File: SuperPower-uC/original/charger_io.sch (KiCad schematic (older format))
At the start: 21 parts, among them J2 Barrel_Jack_Switch, J3 Conn_01x02_Male, Q2 DMP3028LSD, U2 USB-C, U3 IP4220CZ6

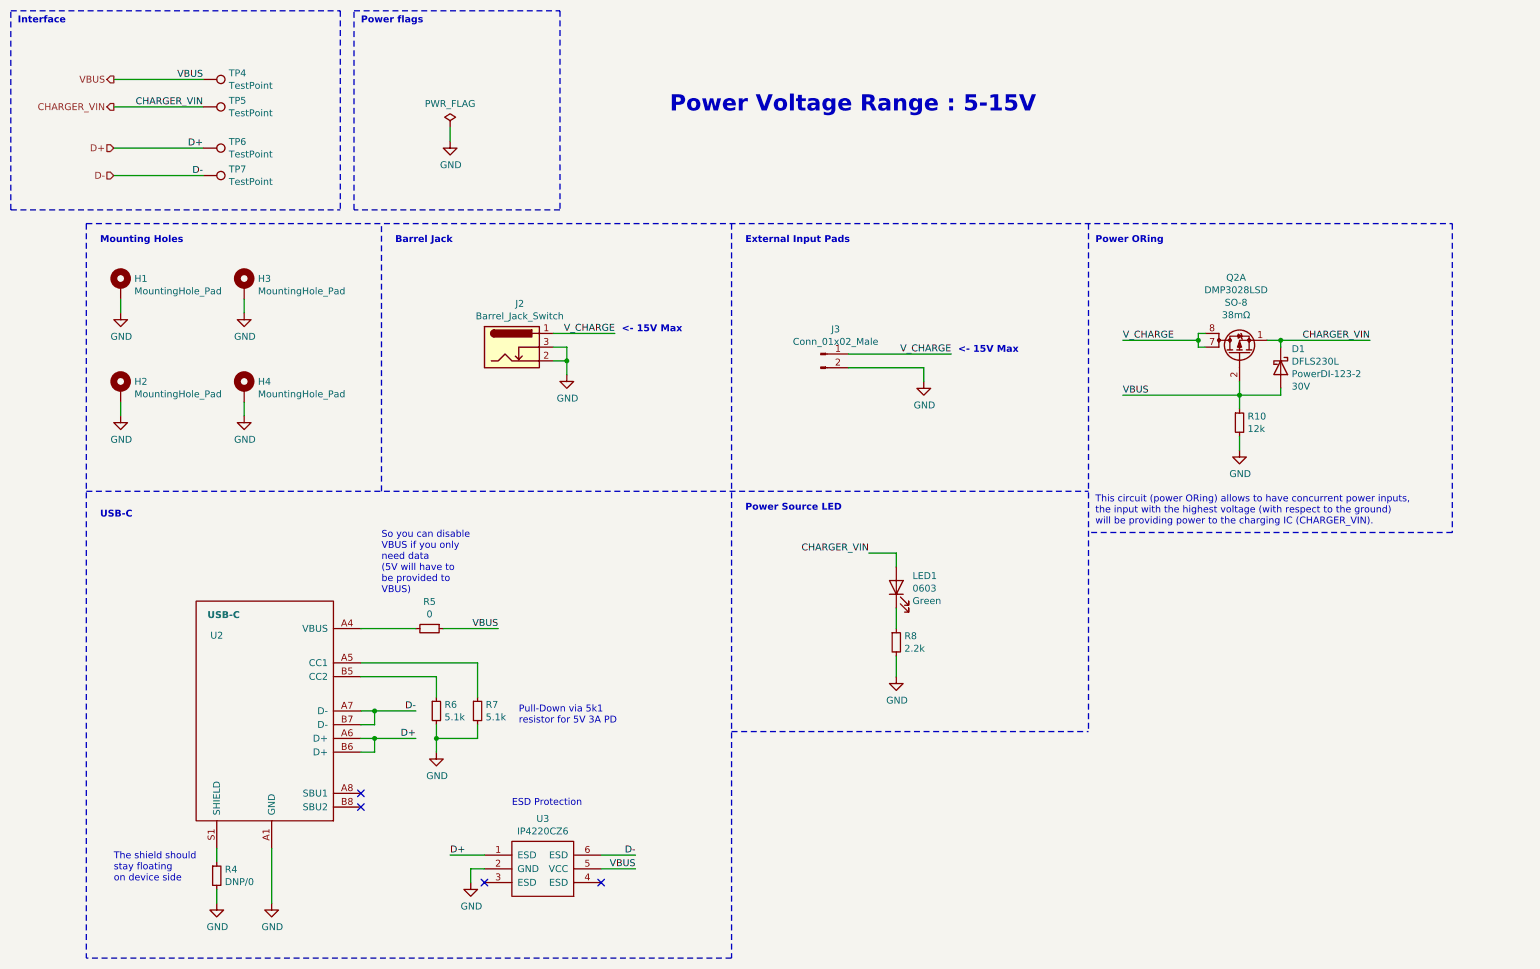
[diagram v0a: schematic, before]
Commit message: Layed out IO sheet parts
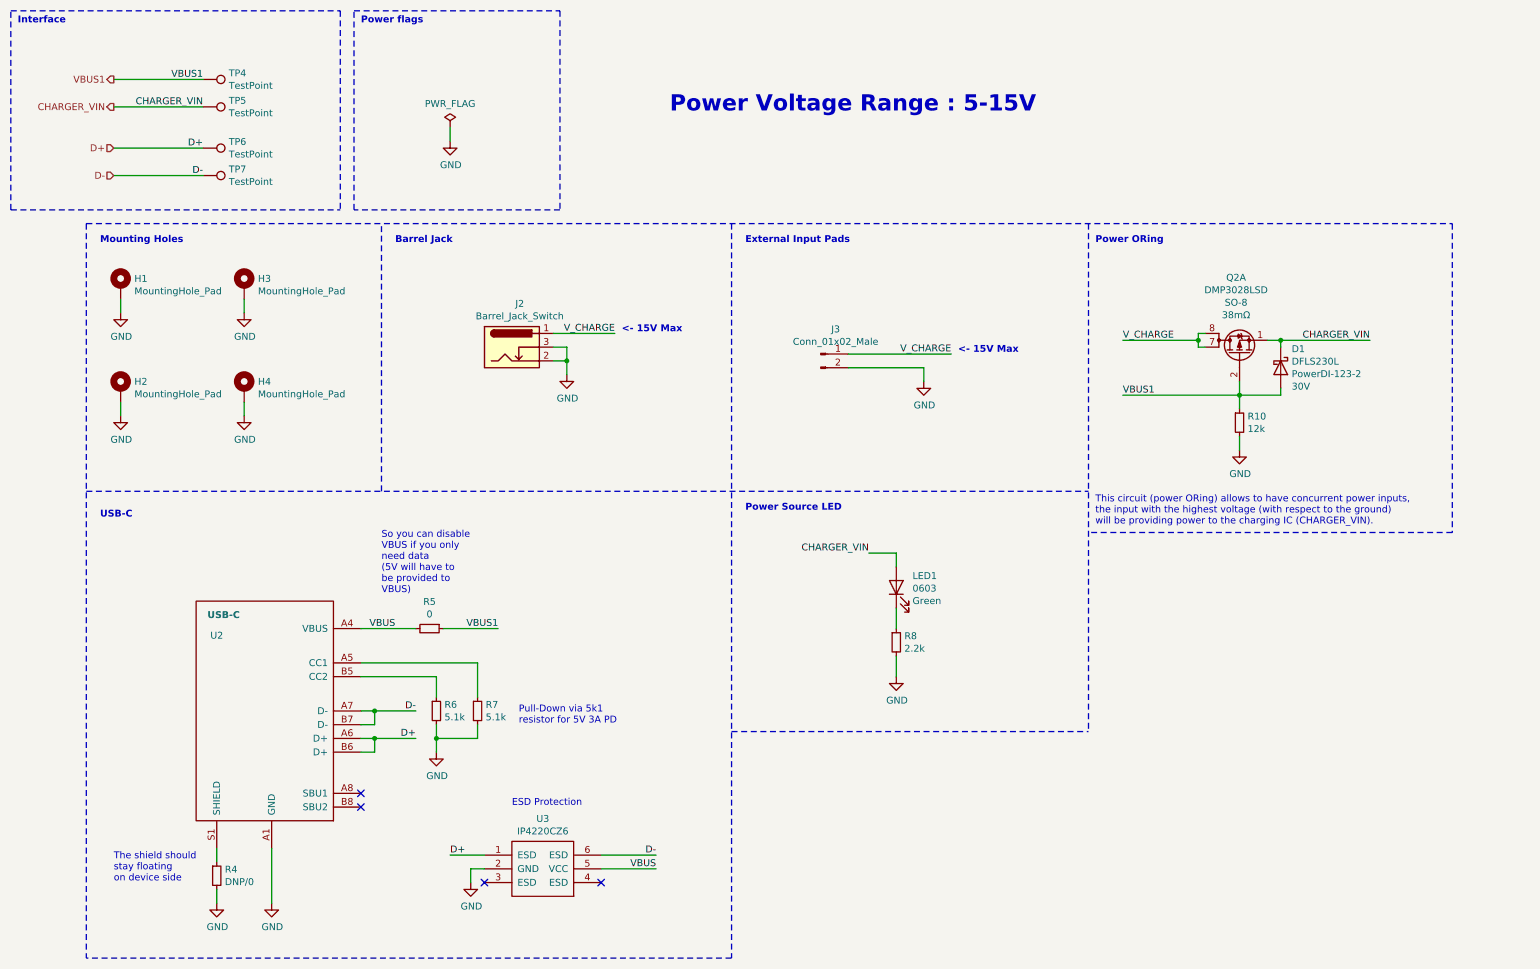
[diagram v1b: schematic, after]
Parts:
- H1, H2, H3, H4: footprint MountingHole:MountingHole_3.2mm_M3_Pad_Via -> MountingHole:MountingHole_2.2mm_M2_Pad_Via
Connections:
- net VBUS: no longer D1.2 (A), Q2.2 (G), R10.1, R5.1, TP4.1
- new net VBUS1: D1.2 (A), Q2.2 (G), R10.1, R5.1, TP4.1
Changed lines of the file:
@@
 $EndDescr
 Text HLabel 1300 1050 0    50   Output ~ 0
-VBUS
+VBUS1
 Text HLabel 1300 1250 0    50   Output ~ 0
 CHARGER_VIN
@@
 D-
 Text Label 4100 5050 2    50   ~ 0
-VBUS
+VBUS1
 Text Label 3500 5650 2    50   ~ 0
 D-
@@
 	4500 2900 4950 2900
 Text Label 1950 1050 2    50   ~ 0
-VBUS
+VBUS1
 Text Label 4950 2900 2    50   ~ 0
 V_CHARGE
@@
 Text Notes 3250 4800 0    50   ~ 0
 So you can disable \nVBUS if you only \nneed data\n(5V will have to\nbe provided to\nVBUS)\n
-Text Label 5100 6800 2    50   ~ 0
+Text Label 5250 6800 2    50   ~ 0
 VBUS
-Wire Wire Line
-	5100 6800 4850 6800
-Text Label 5100 6700 2    50   ~ 0
+Text Label 5250 6700 2    50   ~ 0
 D-
 Text Label 3750 6700 0    50   ~ 0
@@
 NoConn ~ 4850 6900
 NoConn ~ 4000 6900
-Wire Wire Line
-	4850 6700 5100 6700
 Wire Wire Line
 	4000 6700 3750 6700
@@
 Power ORing
 Text Label 8650 3350 0    50   ~ 0
-VBUS
+VBUS1
 Text Notes 8450 4300 0    50   ~ 0
 This circuit (power ORing) allows to have concurrent power inputs,\nthe input with the highest voltage (with respect to the ground)\nwill be providing power to the charging IC (CHARGER_VIN).
@@
 F 0 "H1" H 1450 2599 50  0000 L CNN
 F 1 "MountingHole_Pad" H 1450 2508 50  0000 L CNN
-F 2 "MountingHole:MountingHole_3.2mm_M3_Pad_Via" H 1350 2550 50  0001 C CNN
+F 2 "MountingHole:MountingHole_2.2mm_M2_Pad_Via" H 1350 2550 50  0001 C CNN
 F 3 "~" H 1350 2550 50  0001 C CNN
 	1    1350 2550
@@
 F 0 "H3" H 2350 2599 50  0000 L CNN
 F 1 "MountingHole_Pad" H 2350 2508 50  0000 L CNN
-F 2 "MountingHole:MountingHole_3.2mm_M3_Pad_Via" H 2250 2550 50  0001 C CNN
+F 2 "MountingHole:MountingHole_2.2mm_M2_Pad_Via" H 2250 2550 50  0001 C CNN
 F 3 "~" H 2250 2550 50  0001 C CNN
 	1    2250 2550
@@
 F 0 "H2" H 1450 3349 50  0000 L CNN
 F 1 "MountingHole_Pad" H 1450 3258 50  0000 L CNN
-F 2 "MountingHole:MountingHole_3.2mm_M3_Pad_Via" H 1350 3300 50  0001 C CNN
+F 2 "MountingHole:MountingHole_2.2mm_M2_Pad_Via" H 1350 3300 50  0001 C CNN
 F 3 "~" H 1350 3300 50  0001 C CNN
 	1    1350 3300
@@
 F 0 "H4" H 2350 3349 50  0000 L CNN
 F 1 "MountingHole_Pad" H 2350 3258 50  0000 L CNN
-F 2 "MountingHole:MountingHole_3.2mm_M3_Pad_Via" H 2250 3300 50  0001 C CNN
+F 2 "MountingHole:MountingHole_2.2mm_M2_Pad_Via" H 2250 3300 50  0001 C CNN
 F 3 "~" H 2250 3300 50  0001 C CNN
 	1    2250 3300
@@
 Text Notes 3100 650  0    50   ~ 10
 Power flags
+Wire Wire Line
+	4850 6700 5250 6700
+Wire Wire Line
+	4850 6800 5250 6800
+Text Label 3350 5050 2    50   ~ 0
+VBUS
 $EndSCHEMATC

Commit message: draft of the squared stackable version
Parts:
- H1, H2, H3, H4: footprint MountingHole:MountingHole_2.2mm_M2_Pad_Via -> MountingHole:MountingHole_2.2mm_M2
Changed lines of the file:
@@
 F 0 "H1" H 1450 2599 50  0000 L CNN
 F 1 "MountingHole_Pad" H 1450 2508 50  0000 L CNN
-F 2 "MountingHole:MountingHole_2.2mm_M2_Pad_Via" H 1350 2550 50  0001 C CNN
+F 2 "MountingHole:MountingHole_2.2mm_M2" H 1350 2550 50  0001 C CNN
 F 3 "~" H 1350 2550 50  0001 C CNN
 	1    1350 2550
@@
 F 0 "H3" H 2350 2599 50  0000 L CNN
 F 1 "MountingHole_Pad" H 2350 2508 50  0000 L CNN
-F 2 "MountingHole:MountingHole_2.2mm_M2_Pad_Via" H 2250 2550 50  0001 C CNN
+F 2 "MountingHole:MountingHole_2.2mm_M2" H 2250 2550 50  0001 C CNN
 F 3 "~" H 2250 2550 50  0001 C CNN
 	1    2250 2550
@@
 F 0 "H2" H 1450 3349 50  0000 L CNN
 F 1 "MountingHole_Pad" H 1450 3258 50  0000 L CNN
-F 2 "MountingHole:MountingHole_2.2mm_M2_Pad_Via" H 1350 3300 50  0001 C CNN
+F 2 "MountingHole:MountingHole_2.2mm_M2" H 1350 3300 50  0001 C CNN
 F 3 "~" H 1350 3300 50  0001 C CNN
 	1    1350 3300
@@
 F 0 "H4" H 2350 3349 50  0000 L CNN
 F 1 "MountingHole_Pad" H 2350 3258 50  0000 L CNN
-F 2 "MountingHole:MountingHole_2.2mm_M2_Pad_Via" H 2250 3300 50  0001 C CNN
+F 2 "MountingHole:MountingHole_2.2mm_M2" H 2250 3300 50  0001 C CNN
 F 3 "~" H 2250 3300 50  0001 C CNN
 	1    2250 3300

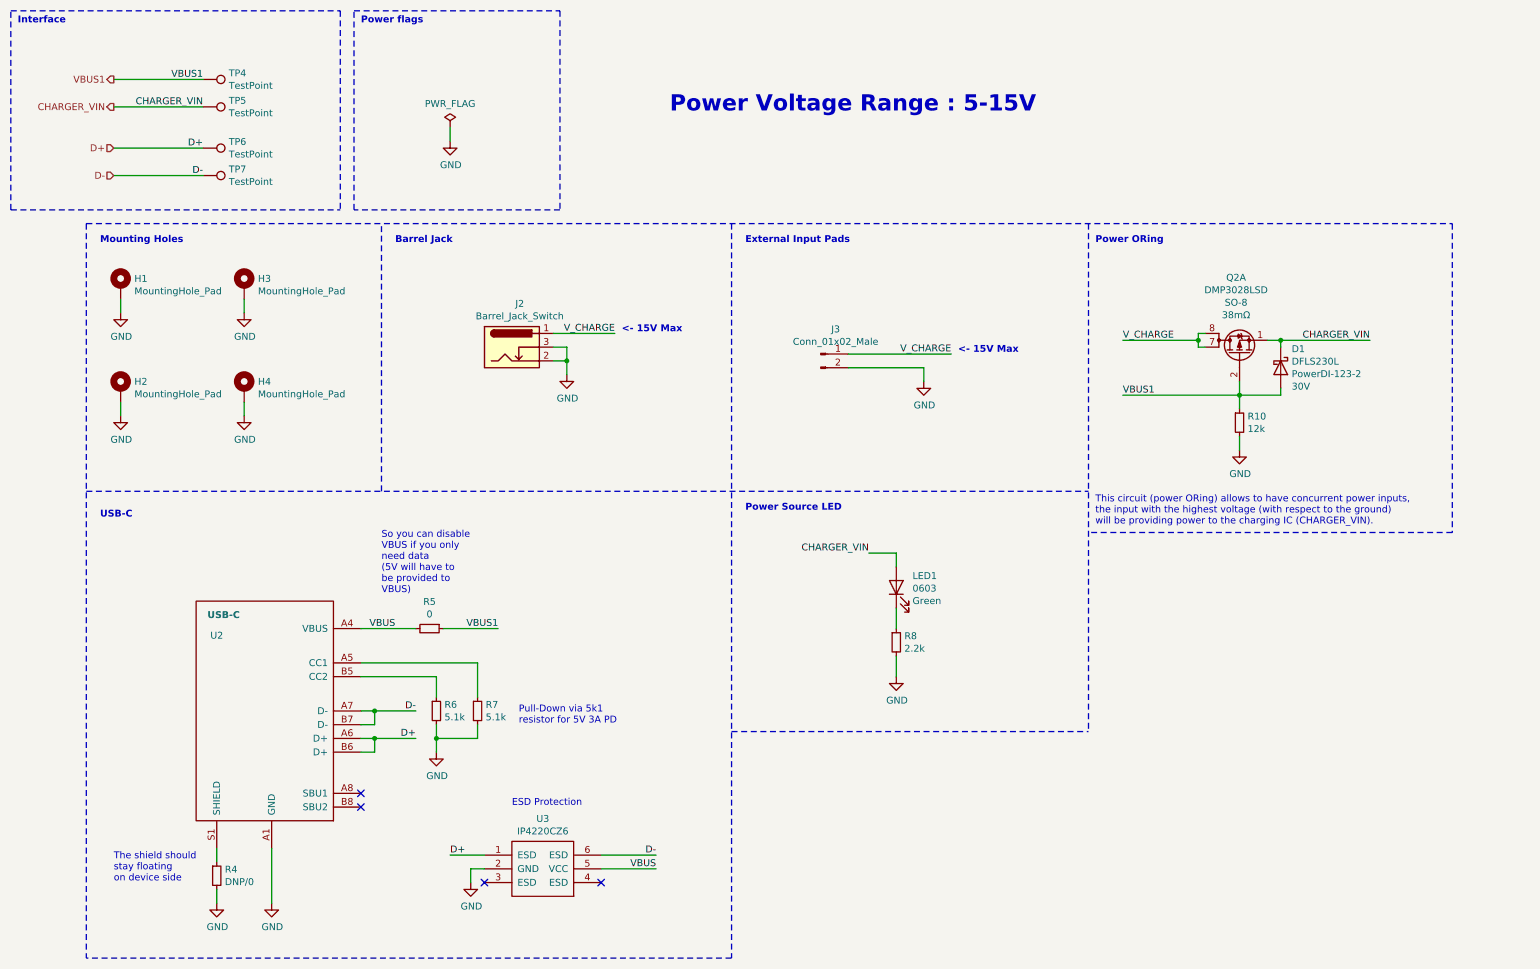
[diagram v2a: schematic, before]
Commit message: Removed 0R from USB-C VBUS because it can not be used as planned and has no function
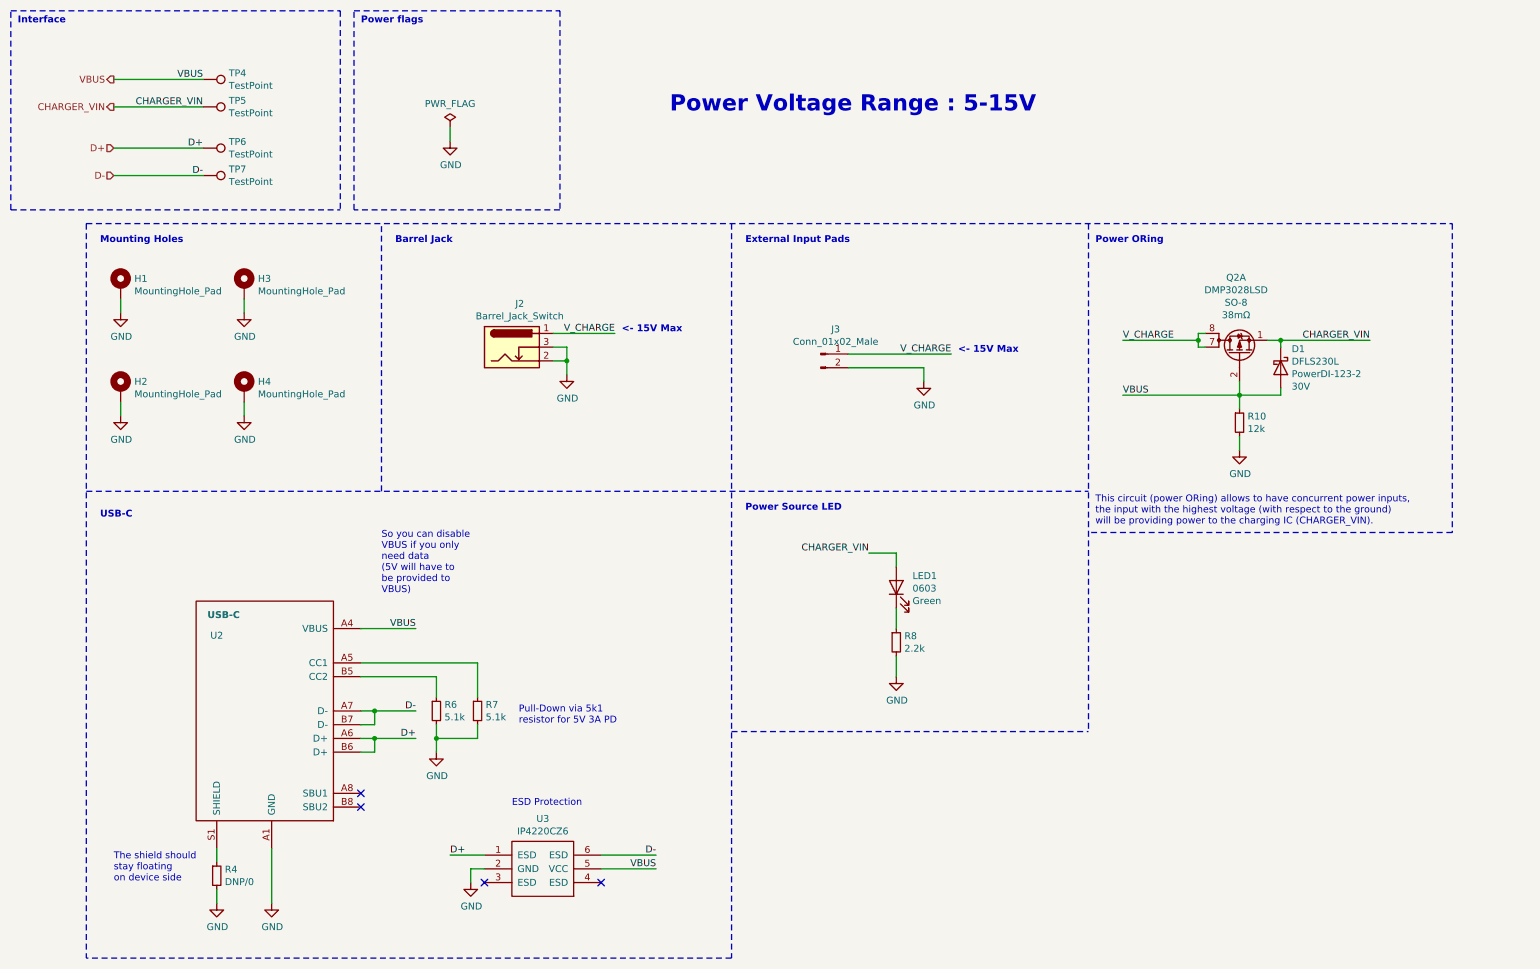
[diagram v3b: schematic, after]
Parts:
- removed R5: 0, Resistor_SMD:R_0603_1608Metric, symbol Device:R_Small
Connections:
- net VBUS1 is gone; now on net VBUS: D1.2 (A), Q2.2 (G), R10.1, TP4.1
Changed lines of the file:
@@
 $EndDescr
 Text HLabel 1300 1050 0    50   Output ~ 0
-VBUS1
+VBUS
 Text HLabel 1300 1250 0    50   Output ~ 0
 CHARGER_VIN
@@
 Text HLabel 1300 1750 0    50   Input ~ 0
 D-
-Text Label 4100 5050 2    50   ~ 0
-VBUS1
 Text Label 3500 5650 2    50   ~ 0
 D-
@@
 Wire Wire Line
 	4500 2900 4950 2900
-Text Label 1950 1050 2    50   ~ 0
-VBUS1
 Text Label 4950 2900 2    50   ~ 0
 V_CHARGE
@@
 Wire Wire Line
 	1950 1250 1300 1250
-Wire Wire Line
-	4100 5050 3700 5050
-$Comp
-L Device:R_Small R5
-U 1 1 5F73032E
-P 3600 5050
-F 0 "R5" V 3404 5050 50  0000 C CNN
-F 1 "0" V 3495 5050 50  0000 C CNN
-F 2 "Resistor_SMD:R_0603_1608Metric" H 3600 5050 50  0001 C CNN
-F 3 "~" H 3600 5050 50  0001 C CNN
-	1    3600 5050
-	0    1    1    0
-$EndComp
 Wire Notes Line
 	3250 4050 3250 2100
@@
 Text Notes 8450 2250 0    50   ~ 10
 Power ORing
-Text Label 8650 3350 0    50   ~ 0
-VBUS1
 Text Notes 8450 4300 0    50   ~ 0
 This circuit (power ORing) allows to have concurrent power inputs,\nthe input with the highest voltage (with respect to the ground)\nwill be providing power to the charging IC (CHARGER_VIN).
@@
 Wire Wire Line
 	4850 6800 5250 6800
-Text Label 3350 5050 2    50   ~ 0
+Text Label 3500 5050 2    50   ~ 0
+VBUS
+Text Label 8650 3350 0    50   ~ 0
+VBUS
+Text Label 1950 1050 2    50   ~ 0
 VBUS
 $EndSCHEMATC
